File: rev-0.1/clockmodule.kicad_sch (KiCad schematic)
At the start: 41 parts, among them J3 DC Input, SW1 SW_Push, SW2 SW_Push, U1 NE555P, U3 L7805_J, U6 NE555P, U7 NE555P, U8 7400

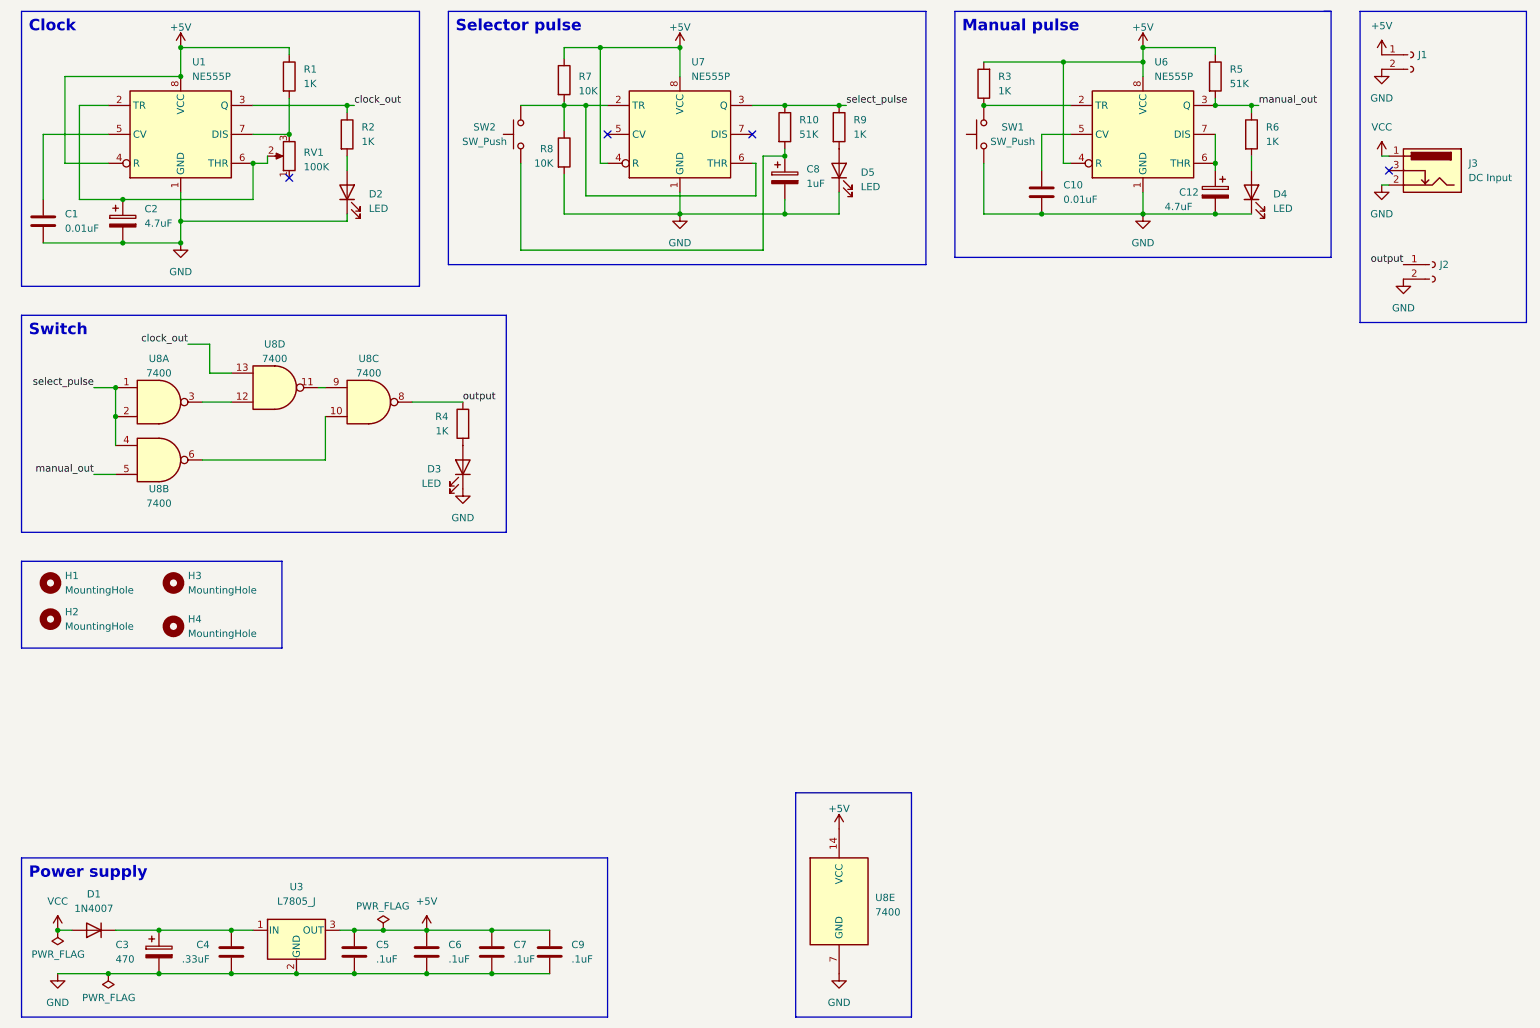
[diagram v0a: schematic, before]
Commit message: Swapped C4 and C3 silkscreen text
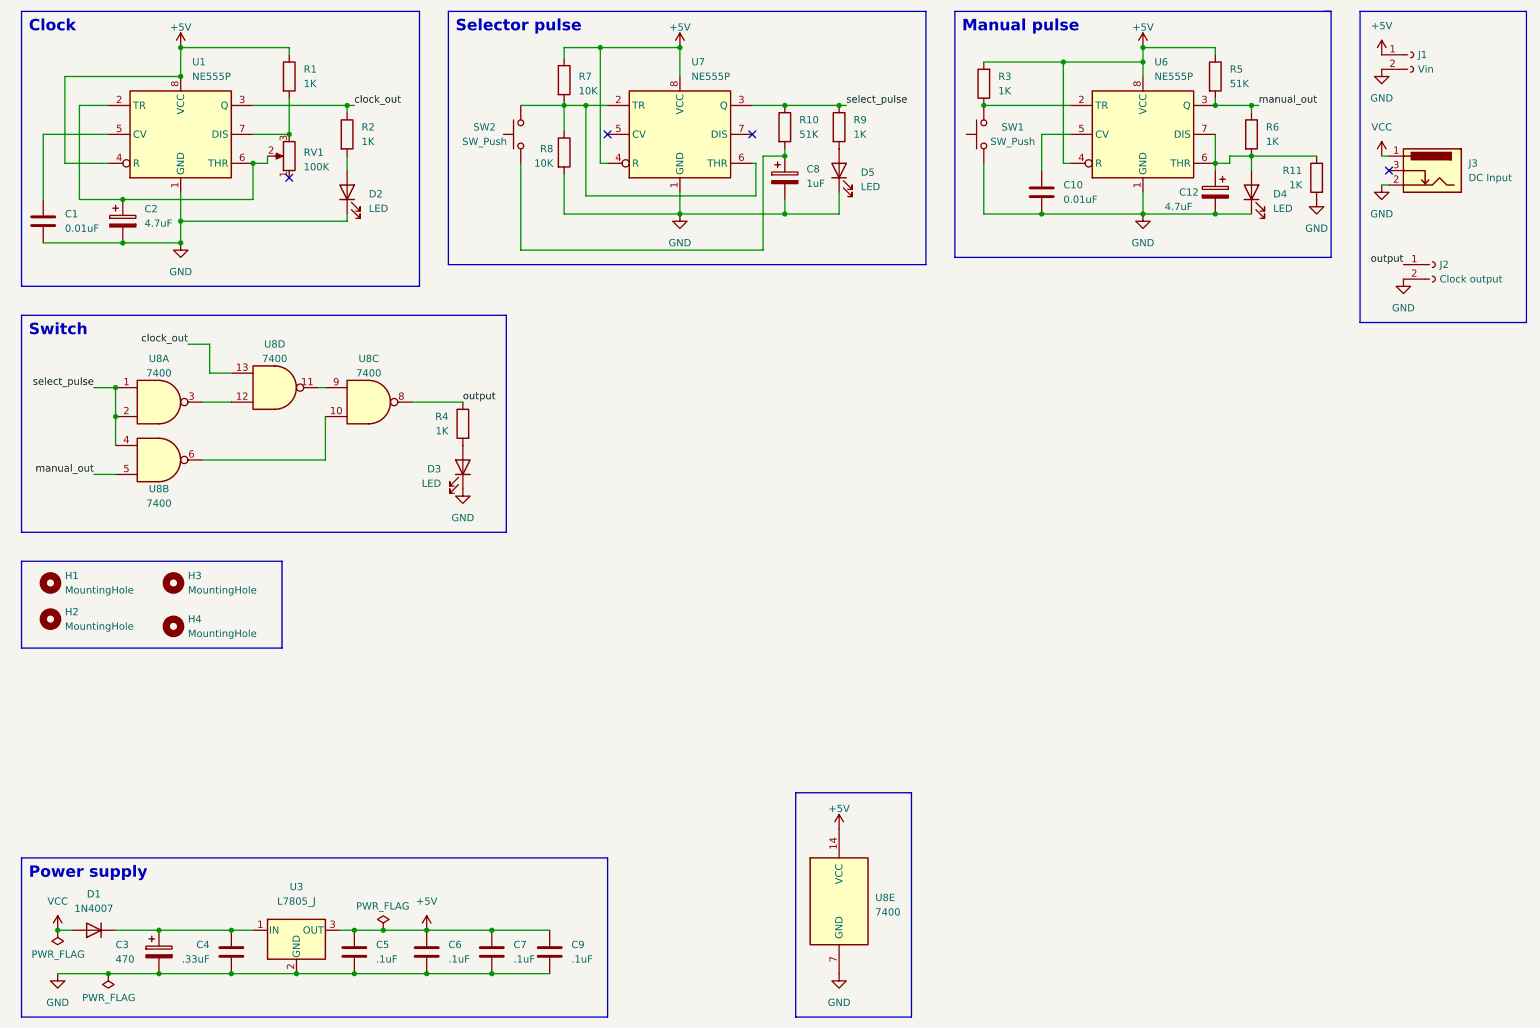
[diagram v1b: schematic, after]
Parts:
- added R11: 1K, Resistor_THT:R_Axial_DIN0204_L3.6mm_D1.6mm_P7.62mm_Horizontal, symbol Device:R
- J1: value (none) -> Vin
- J2: value (none) -> Clock output
- RV1: footprint (none) -> w_pth_resistors:trimmer_alps-rk09k1130ah1
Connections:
- net GND: now also R11.2
- net at C12.1, U6.6 (THR), U6.7 (DIS): now also D4.2 (A), R6.2, R11.1

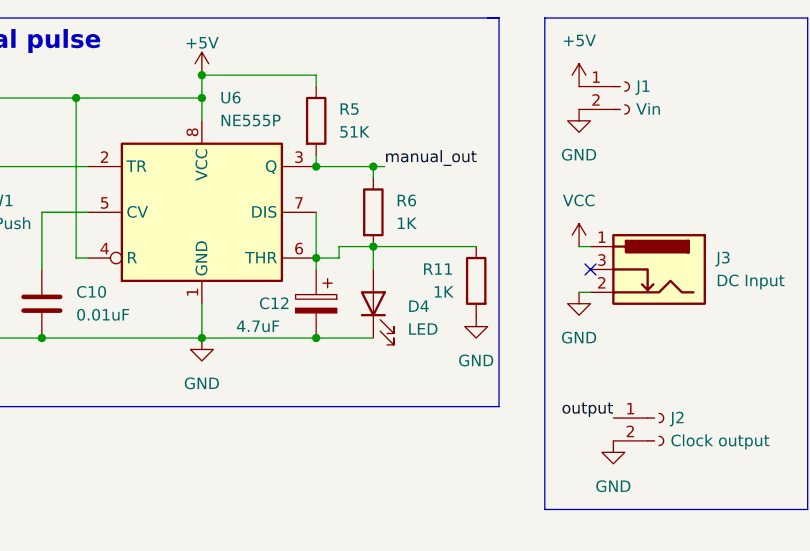
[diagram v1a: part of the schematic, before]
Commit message: Moved `R11`
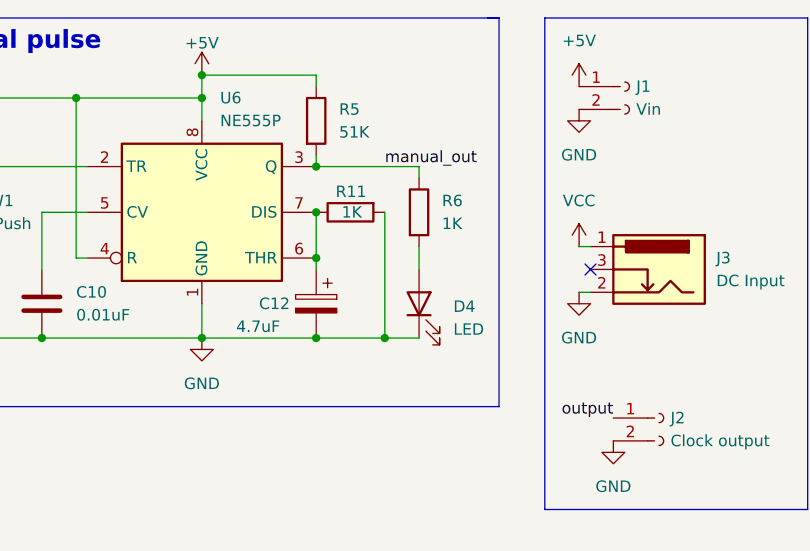
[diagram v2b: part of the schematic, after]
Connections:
- net at C12.1, R11.1, U6.6 (THR)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: no longer D4.2 (A), R6.2
- new net: D4.2 (A), R6.2
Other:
- moved on the sheet: D4, R11, R6
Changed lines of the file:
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@@
 	)
 	(junction
-		(at 232.41 33.02)
-		(diameter 0)
-		(color 0 0 0 0)
-	)
-	(junction
 		(at 22.86 177.8)
 		(diameter 0)
@@
 	)
 	(junction
+		(at 233.68 52.07)
+		(diameter 0)
+		(color 0 0 0 0)
+	)
+	(junction
 		(at 213.36 22.86)
 		(diameter 0)
@@
 	)
 	(junction
+		(at 226.06 38.1)
+		(diameter 0)
+		(color 0 0 0 0)
+	)
+	(junction
 		(at 185.42 33.02)
 		(diameter 0)
@@
 	)
 	(junction
-		(at 232.41 41.91)
-		(diameter 0)
-		(color 0 0 0 0)
-	)
-	(junction
 		(at 87.63 177.8)
 		(diameter 0)
@@
 		)
 	)
+	(wire
+		(pts
+			(xy 233.68 38.1) (xy 233.68 52.07)
+		)
+		(stroke
+			(width 0)
+			(type default)
+		)
+	)
 	(polyline
 		(pts
@@
 	(wire
 		(pts
-			(xy 226.06 33.02) (xy 232.41 33.02)
+			(xy 226.06 33.02) (xy 237.49 33.02)
 		)
 		(stroke
@@
 	(wire
 		(pts
-			(xy 226.06 52.07) (xy 232.41 52.07)
+			(xy 226.06 52.07) (xy 233.68 52.07)
 		)
 		(stroke
@@
 	(wire
 		(pts
-			(xy 232.41 41.91) (xy 228.6 41.91)
-		)
-		(stroke
-			(width 0)
-			(type default)
-		)
-	)
-	(wire
-		(pts
 			(xy 33.02 82.55) (xy 33.02 87.63)
 		)
@@
 	(wire
 		(pts
-			(xy 232.41 44.45) (xy 232.41 41.91)
+			(xy 237.49 44.45) (xy 237.49 41.91)
 		)
 		(stroke
@@
 		)
 	)
-	(wire
-		(pts
-			(xy 228.6 41.91) (xy 228.6 43.18)
-		)
-		(stroke
-			(width 0)
-			(type default)
-		)
-	)
 	(polyline
 		(pts
@@
 	(wire
 		(pts
-			(xy 232.41 34.29) (xy 232.41 33.02)
+			(xy 237.49 34.29) (xy 237.49 33.02)
 		)
 		(stroke
@@
 	(wire
 		(pts
-			(xy 232.41 33.02) (xy 233.68 33.02)
-		)
-		(stroke
-			(width 0)
-			(type default)
-		)
-	)
-	(wire
-		(pts
 			(xy 57.15 43.18) (xy 57.15 49.53)
 		)
@@
 		)
 	)
-	(wire
-		(pts
-			(xy 243.84 41.91) (xy 232.41 41.91)
-		)
-		(stroke
-			(width 0)
-			(type default)
-		)
-	)
 	(polyline
 		(pts
@@
 		)
 	)
-	(wire
-		(pts
-			(xy 228.6 43.18) (xy 226.06 43.18)
-		)
-		(stroke
-			(width 0)
-			(type default)
-		)
-	)
 	(polyline
 		(pts
@@
 		)
 	)
+	(wire
+		(pts
+			(xy 233.68 52.07) (xy 237.49 52.07)
+		)
+		(stroke
+			(width 0)
+			(type default)
+		)
+	)
 	(text "Power supply"
 		(exclude_from_sim no)
@@
 	(symbol
 		(lib_id "Device:R")
-		(at 232.41 38.1 0)
+		(at 237.49 38.1 0)
 		(unit 1)
 		(exclude_from_sim no)
@@
 		(fields_autoplaced yes)
 		(property "Reference" "R6"
-			(at 234.95 36.8299 0)
+			(at 240.03 36.8299 0)
 			(effects
 				(font
@@
 		)
 		(property "Value" "1K"
-			(at 234.95 39.3699 0)
+			(at 240.03 39.3699 0)
 			(effects
 				(font
@@
 		)
 		(property "Footprint" "Resistor_THT:R_Axial_DIN0204_L3.6mm_D1.6mm_P7.62mm_Horizontal"
-			(at 230.632 38.1 90)
+			(at 235.712 38.1 90)
 			(effects
 				(font
@@
 		)
 		(property "Datasheet" "~"
-			(at 232.41 38.1 0)
+			(at 237.49 38.1 0)
 			(effects
 				(font
@@
 		)
 		(property "Description" ""
-			(at 232.41 38.1 0)
+			(at 237.49 38.1 0)
 			(effects
 				(font
@@
 	(symbol
 		(lib_id "Device:LED")
-		(at 232.41 48.26 90)
+		(at 237.49 48.26 90)
 		(unit 1)
 		(exclude_from_sim no)
@@
 		(dnp no)
 		(property "Reference" "D4"
-			(at 236.22 48.5774 90)
+			(at 241.3 48.5774 90)
 			(effects
 				(font
@@
 		)
 		(property "Value" "LED"
-			(at 236.22 51.1174 90)
+			(at 241.3 51.1174 90)
 			(effects
 				(font
@@
 		)
 		(property "Footprint" "LED_THT:LED_D5.0mm"
-			(at 232.41 48.26 0)
+			(at 237.49 48.26 0)
 			(effects
 				(font
@@
 		)
 		(property "Datasheet" "~"
-			(at 232.41 48.26 0)
+			(at 237.49 48.26 0)
 			(effects
 				(font
@@
 		)
 		(property "Description" ""
-			(at 232.41 48.26 0)
+			(at 237.49 48.26 0)
 			(effects
 				(font
@@
 	(symbol
 		(lib_id "Device:R")
-		(at 243.84 45.72 0)
-		(mirror y)
+		(at 229.87 38.1 90)
+		(mirror x)
 		(unit 1)
 		(exclude_from_sim no)
@@
 		(dnp no)
 		(property "Reference" "R11"
-			(at 241.3 44.4499 0)
+			(at 231.648 35.814 90)
 			(effects
 				(font
@@
 		)
 		(property "Value" "1K"
-			(at 241.3 46.9899 0)
+			(at 231.14 38.1 90)
 			(effects
 				(font
@@
 		)
 		(property "Footprint" "Resistor_THT:R_Axial_DIN0204_L3.6mm_D1.6mm_P7.62mm_Horizontal"
-			(at 245.618 45.72 90)
+			(at 229.87 36.322 90)
 			(effects
 				(font
@@
 		)
 		(property "Datasheet" "~"
-			(at 243.84 45.72 0)
+			(at 229.87 38.1 0)
 			(effects
 				(font
@@
 		)
 		(property "Description" ""
-			(at 243.84 45.72 0)
+			(at 229.87 38.1 0)
 			(effects
 				(font
@@
 					(unit 1)
 				)
-			)
-		)
-	)
-	(symbol
-		(lib_id "power:GND")
-		(at 243.84 49.53 0)
-		(unit 1)
-		(exclude_from_sim no)
-		(in_bom yes)
-		(on_board yes)
-		(dnp no)
-		(fields_autoplaced yes)
-		(property "Reference" "#PWR05"
-			(at 243.84 55.88 0)
-			(effects
-				(font
-					(size 1.27 1.27)
-				)
-				(hide yes)
-			)
-		)
-		(property "Value" "GND"
-			(at 243.84 54.61 0)
-			(effects
-				(font
-					(size 1.27 1.27)
-				)
-			)
-		)
-		(property "Footprint" ""
-			(at 243.84 49.53 0)
-			(effects
-				(font
-					(size 1.27 1.27)
-				)
-				(hide yes)
-			)
-		)
-		(property "Datasheet" ""
-			(at 243.84 49.53 0)
-			(effects
-				(font
-					(size 1.27 1.27)
-				)
-				(hide yes)
-			)
-		)
-		(property "Description" ""
-			(at 243.84 49.53 0)
-			(effects
-				(font
-					(size 1.27 1.27)
-				)
-				(hide yes)
-			)
-		)
-		(pin "1"
-		)
-		(instances
-			(project "clockmodule"
-				(path "/9538e4ed-27e6-4c37-b989-9859dc0d49e8"
-					(reference "#PWR05")
-					(unit 1)
-				)

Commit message: Change `C8` footprint
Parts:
- C8: footprint Capacitor_THT:C_Disc_D3.0mm_W1.6mm_P2.50mm -> Capacitor_THT:CP_Radial_D4.0mm_P1.50mm
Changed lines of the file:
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@@
 			)
 		)
-		(property "Footprint" "Capacitor_THT:C_Disc_D3.0mm_W1.6mm_P2.50mm"
+		(property "Footprint" "Capacitor_THT:CP_Radial_D4.0mm_P1.50mm"
 			(at 151.4602 49.53 0)
 			(effects
